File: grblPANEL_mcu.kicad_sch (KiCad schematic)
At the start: 31 parts, among them J201 2x5x1.27mm, J202 USB_C_Receptacle_USB2.0, SW201 SW_Push, SW202 SW_Push, U201 STM32G0B1CxTxN, U202 USBLC6-2SC6, Y201 8MHz

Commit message: small cleanups
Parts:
- C206, C207: value 10p -> 16p
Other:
- note added: "LCSC#: C518155 Mfr.#: 3225-8.00-12-10-10/A Mfr: Suzhou Liming Elec 8MHz SMD Crystal Resonator 12pF ±10ppm ±10ppm SMD3225-4P Crystals ROHS"
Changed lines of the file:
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@@
+    (effects (font (size 1.27 1.27)) (justify left bottom))
+  )
+  (text "LCSC#: C518155\nMfr.#: 3225-8.00-12-10-10/A\nMfr: Suzhou Liming Elec\n8MHz SMD Crystal Resonator 12pF ±10ppm ±10ppm\nSMD3225-4P Crystals ROHS"
+    (at 121.92 160.02 0)
     (effects (font (size 1.27 1.27)) (justify left bottom))
   )
@@
       (effects (font (size 1.27 1.27)) (justify left))
     )
-    (property "Value" "10p" (id 1) (at 167.64 139.7 0)
+    (property "Value" "16p" (id 1) (at 167.64 139.7 0)
       (effects (font (size 1.27 1.27)) (justify left))
     )
@@
       (effects (font (size 1.27 1.27)) (justify left))
     )
-    (property "Value" "10p" (id 1) (at 142.24 139.7 0)
-      (effects (font (size 1.27 1.27)) (justify left))
-    )
+    (property "Value" "16p" (id 1) (at 142.24 139.7 0)
+      (effects (font (size 1.27 1.27)) (justify left))
+    )

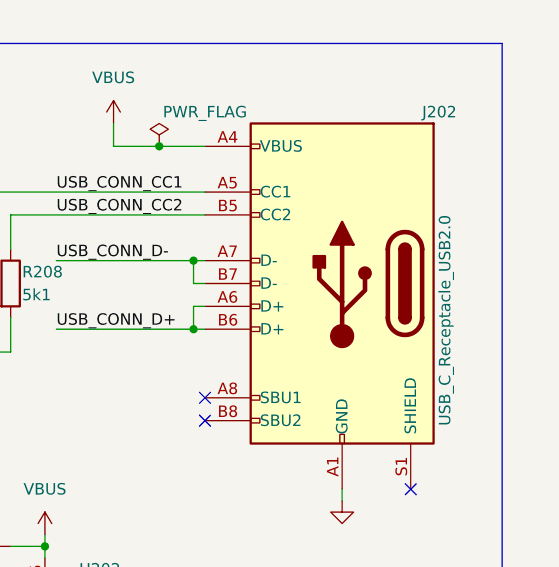
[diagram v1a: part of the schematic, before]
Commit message: v7 upgrade
schematic symbols updated from libraries

pcb update from schematic
update footprints from library

board setup, thermal relief count

still DRC warnings where symbols have been updated locally with 3d
models etc

copper sliver warning from zone fill
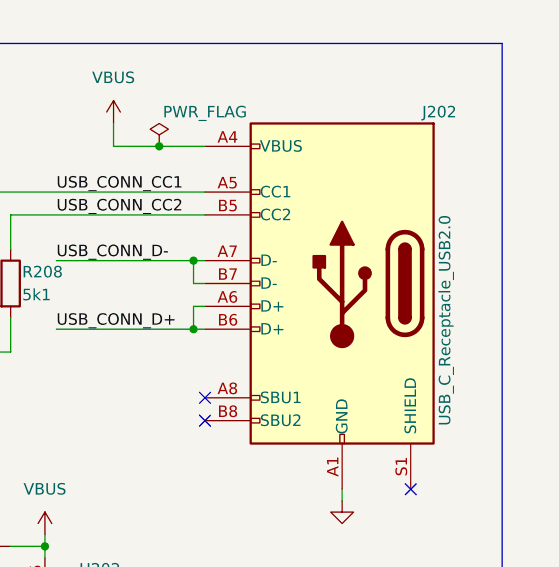
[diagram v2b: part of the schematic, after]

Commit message: Schematic: add usart6 connector on pa4/pa5
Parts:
- added J203: USART6, symbol Connector_Generic:Conn_01x02
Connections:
- net at U201.15 (PA4): now also J203.1 (Pin_1)
- net at U201.16 (PA5): now also J203.2 (Pin_2)
- no-connect marks 19 -> 17
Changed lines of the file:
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@@
   )
   (no_connect (at 241.3 116.84))
-  (no_connect (at 78.74 81.28))
-  (no_connect (at 78.74 78.74))
   (no_connect (at 116.84 73.66))
   (no_connect (at 116.84 66.04))
@@
     (stroke (width 0) (type default))
   )
+  (wire (pts (xy 71.12 81.28) (xy 78.74 81.28))
+    (stroke (width 0) (type default))
+  )
   (wire (pts (xy 241.3 104.14) (xy 240.03 104.14))
     (stroke (width 0) (type default))
@@
   )
   (wire (pts (xy 96.52 129.54) (xy 96.52 134.62))
+    (stroke (width 0) (type default))
+  )
+  (wire (pts (xy 71.12 78.74) (xy 78.74 78.74))
     (stroke (width 0) (type default))
   )
@@
         )
       )
+    )
+  )
+  (symbol (lib_id "Connector_Generic:Conn_01x02") (at 66.04 78.74 0) (mirror y) (unit 1)
+    (in_bom yes) (on_board yes) (dnp no)
+    (property "Reference" "J203" (at 64.77 78.74 0)
+      (effects (font (size 1.27 1.27)) (justify left))
+    )
+    (property "Value" "USART6" (at 64.77 81.28 0)
+      (effects (font (size 1.27 1.27)) (justify left))
+    )
+    (property "Footprint" "" (at 66.04 78.74 0)
+      (effects (font (size 1.27 1.27)) hide)
+    )
+    (property "Datasheet" "~" (at 66.04 78.74 0)
+      (effects (font (size 1.27 1.27)) hide)
+    )
+    (pin "1")
+    (pin "2")
+    (instances
+      (project "grblPANEL"
+        (path "/1f77927e-2ca9-4002-a421-c6796d5f0016/437f2ceb-712b-41a0-9e79-c6c2becba629"
+          (reference "J203") (unit 1)
+        )
+      )

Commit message: Add power protection status LEDs
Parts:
- removed J203: USART6, symbol Connector_Generic:Conn_01x02
- added TP201, TP202: TestPoint, TestPoint:TestPoint_THTPad_D2.0mm_Drill1.0mm, symbol Connector:TestPoint
- D201: footprint LED_SMD:LED_0603_1608Metric -> LED_SMD:LED_1206_3216Metric_ReverseMount_Hole1.8x2.4mm
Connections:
- net at U201.15 (PA4): now also TP201.1
- net at U201.16 (PA5): now also TP202.1

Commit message: Place and route changes from schematic
Headers for serial console.
DNP components to v7 format.
Power status components.
LEDs to bottom side, plus silkscreen.
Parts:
- D201: footprint LED_SMD:LED_1206_3216Metric_ReverseMount_Hole1.8x2.4mm -> LED_SMD:LED_0603_1608Metric
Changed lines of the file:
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@@
       (effects (font (size 1.27 1.27)) (justify right))
     )
-    (property "Footprint" "LED_SMD:LED_1206_3216Metric_ReverseMount_Hole1.8x2.4mm" (at 135.89 55.88 0)
+    (property "Footprint" "LED_SMD:LED_0603_1608Metric" (at 135.89 55.88 0)
       (effects (font (size 1.27 1.27)) hide)
     )
